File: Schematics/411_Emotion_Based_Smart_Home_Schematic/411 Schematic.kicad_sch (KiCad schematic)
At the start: 12 parts, among them J1 Barrel_Jack, Q1 IRLB8721PBF, U1 LD1117S33TR_SOT223, U3 HC-SR04

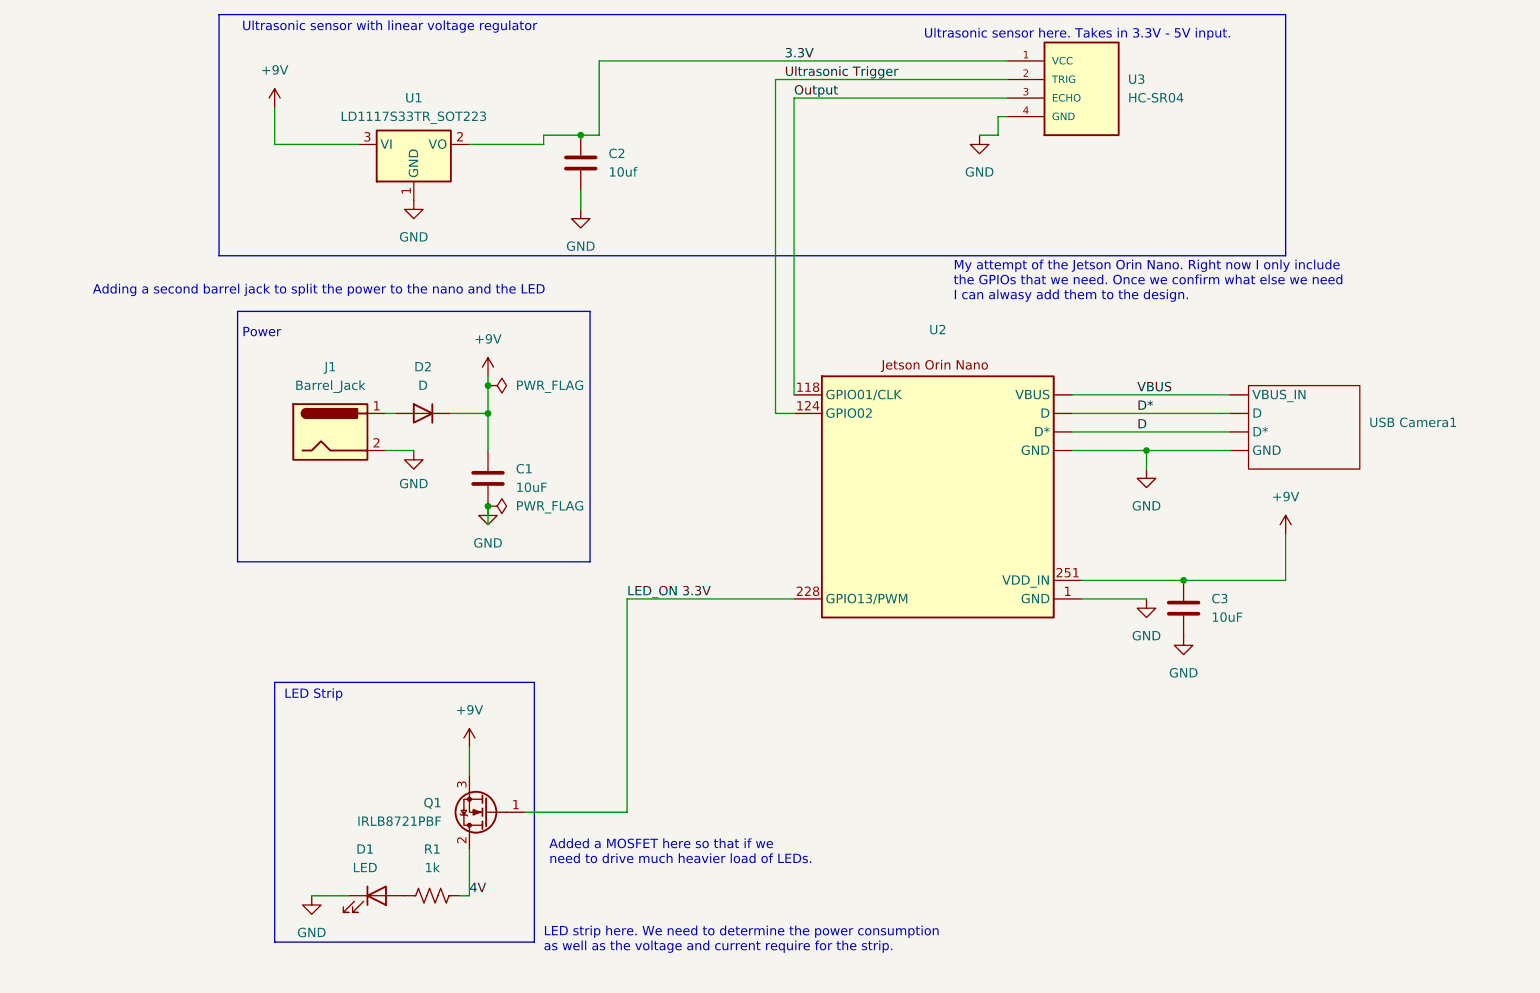
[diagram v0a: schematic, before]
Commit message: Updating what I have of schematic
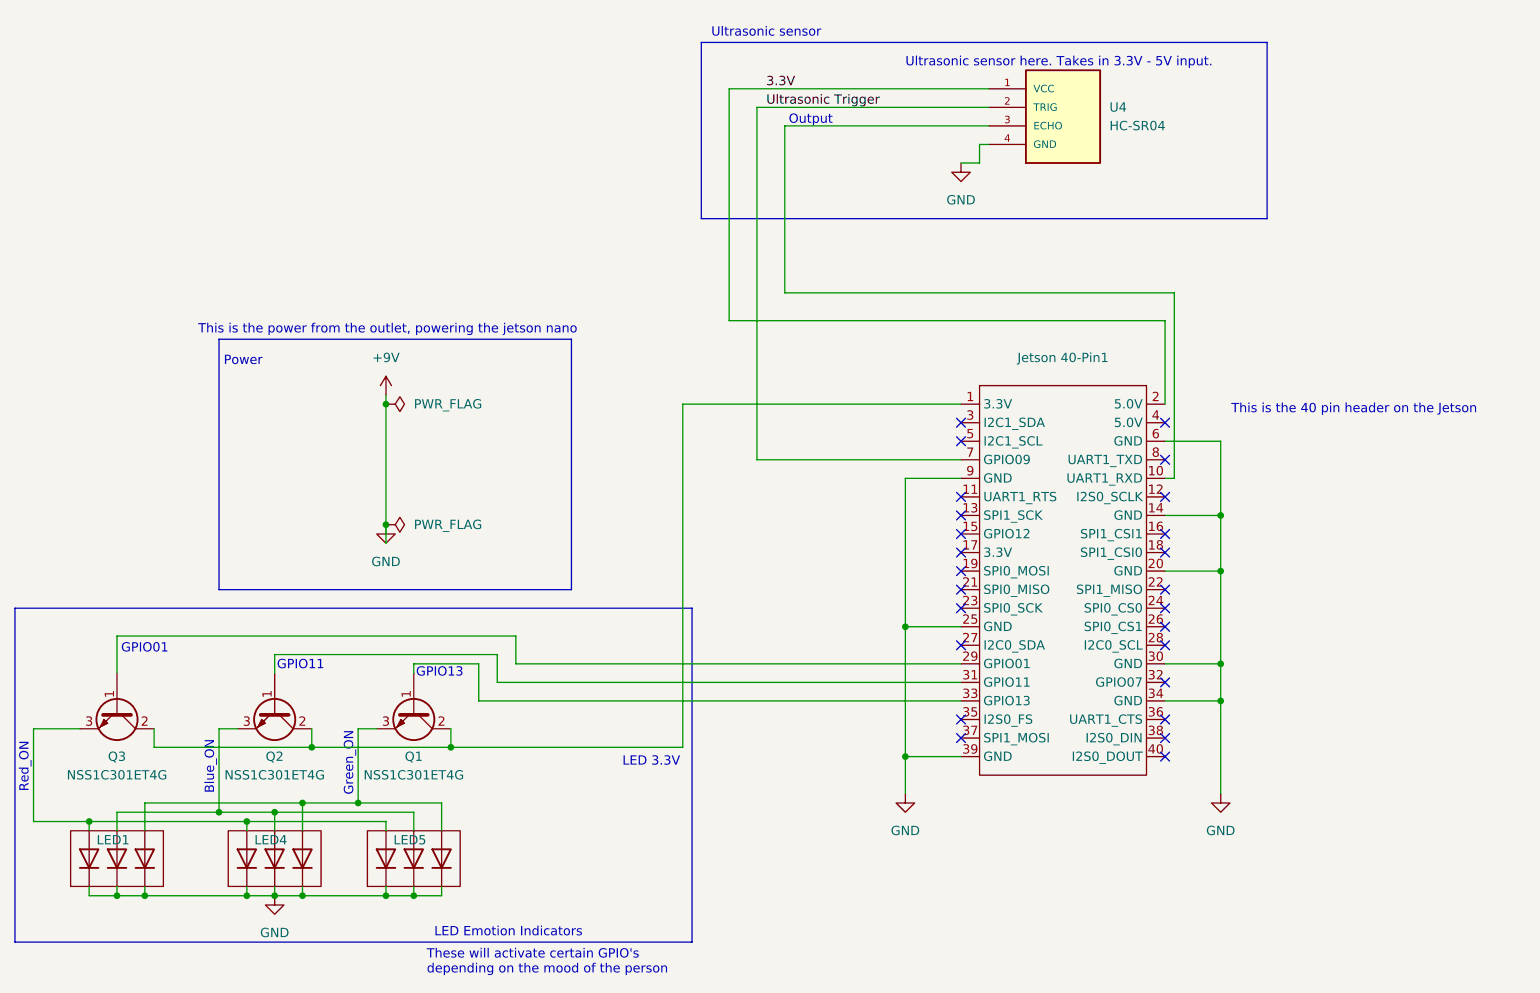
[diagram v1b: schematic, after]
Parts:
- removed C1, C3: 10uF, Capacitor_SMD:CP_Elec_3x5.3, symbol Device:C
- removed C2: 10uf, Capacitor_SMD:CP_Elec_3x5.3, symbol Device:C
- removed D1: LED, LED_SMD:LED-APA102-2020, symbol Device:LED
- removed D2: D, symbol Device:D
- removed J1: Barrel_Jack, Connector_BarrelJack:BarrelJack_CLIFF_FC681465S_SMT_Horizontal, symbol Connector:Barrel_Jack
- removed Q1: IRLB8721PBF, Package_TO_SOT_THT:TO-220-3_Vertical, symbol Transistor_FET:IRLB8721PBF
- removed R1: 1k, symbol Device:R_US
- removed U1: LD1117S33TR_SOT223, Package_TO_SOT_SMD:SOT-223-3_TabPin2, symbol Regulator_Linear:LD1117S33TR_SOT223
- removed U2: ~, symbol jetson_orin_nano:Jetson_Orin_Nano
- removed U3: HC-SR04, HC-SR04:XCVR_HC-SR04, symbol HC-SR04:HC-SR04
- removed USB Camera1: ~, symbol CameraModule:USB_Camera
- added Jetson 40-Pin1: ~, symbol JetsonNano40pin:JetsonNano40pin
- added LED1, LED4, LED5: ~, symbol Device:D
- added Q1, Q2, Q3: NSS1C301ET4G, symbol Device:Q_NPN_BCE
- added U4: HC-SR04, HC-SR04:XCVR_HC-SR04, symbol HC-SR04:HC-SR04
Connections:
- net +9V: now also Jetson 40-Pin1.14 (GND), Jetson 40-Pin1.20 (GND), Jetson 40-Pin1.25 (GND), Jetson 40-Pin1.30 (GND), Jetson 40-Pin1.34 (GND), Jetson 40-Pin1.39 (GND), Jetson 40-Pin1.6 (GND), Jetson 40-Pin1.9 (GND), LED1.4 (K), LED1.5 (K_2), LED1.6 (K_3), LED4.4 (K), LED4.5 (K_2), LED4.6 (K_3), LED5.4 (K), LED5.5 (K_2), LED5.6 (K_3), U4.4 (GND)
- net 3.3V: now also Jetson 40-Pin1.2 (5.0V), U4.1 (VCC)
- net Ultrasonic Trigger: now also Jetson 40-Pin1.7 (GPIO09), U4.2 (TRIG)
- new net: LED1.1 (A), LED4.1 (A), LED5.1 (A), Q3.3 (E)
- new net: LED1.2 (A), LED4.2 (A), LED5.2 (A), Q2.3 (E)
- new net: LED1.3 (A), LED4.3 (A), LED5.3 (A), Q1.3 (E)
- new net: Jetson 40-Pin1.29 (GPIO01), Q3.1 (B)
- new net: Jetson 40-Pin1.1 (3.3V), Q1.2 (C), Q2.2 (C), Q3.2 (C)
- new net: Jetson 40-Pin1.10 (UART1_RXD), U4.3 (ECHO)
- new net: Jetson 40-Pin1.31 (GPIO11), Q2.1 (B)
- new net: Jetson 40-Pin1.33 (GPIO13), Q1.1 (B)
- no-connect marks 0 -> 25
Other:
- note added: "Blue_ON"
- note added: "GPIO01"
- note added: "GPIO11"
- note added: "GPIO13"
- note added: "Green_ON"
- note added: "LED 3.3V"
- note added: "LED Emotion Indicators"
- note added: "Output"
- note added: "Red_ON"
- note added: "These will activate certain GPIO's depending on the mood of the person"
- note added: "This is the 40 pin header on the Jetson"
- note added: "This is the power from the outlet, powering the jetson nano"
- note added: "Ultrasonic sensor"
- note removed: "Added a MOSFET here so that if we need to drive much heavier load of LEDs."
- note removed: "Adding a second barrel jack to split the power to the nano and the LED"
- note removed: "LED Strip"
- note removed: "LED strip here. We need to determine the power consumption as well as the voltage and current require for the strip."
- note removed: "My attempt of the Jetson Orin Nano. Right now I only include the GPIOs that we need. Once we confirm what else we need I can alwasy add them to the design."
- note removed: "Ultrasonic sensor with linear voltage regulator"
